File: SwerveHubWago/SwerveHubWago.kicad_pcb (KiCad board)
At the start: 2 copper layers, 84.5 x 32 mm, 5 parts, among them J1 2601-1110, J2 2601-1104, J3 15-91-3024

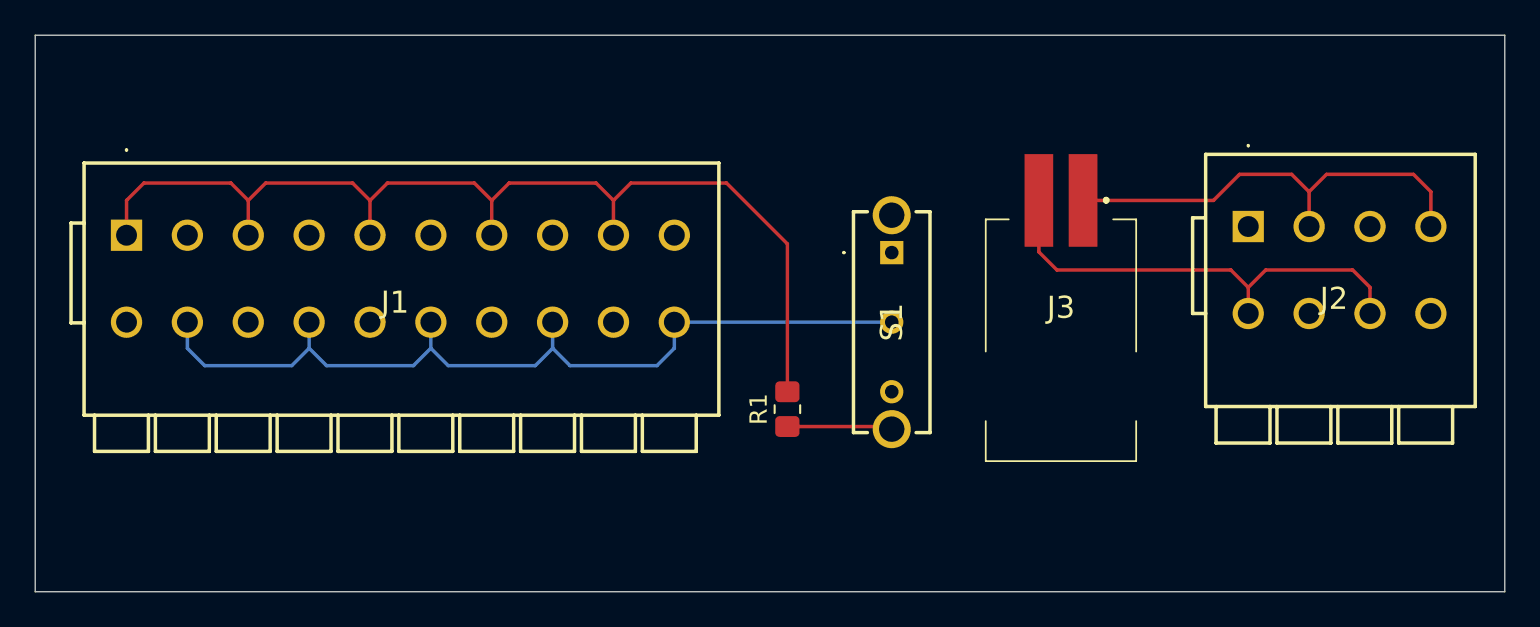
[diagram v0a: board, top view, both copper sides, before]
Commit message: Rev 2
Switched connecters to two (in/out) Molex SL connectors for CAN and one three pin Molex SL connector for power. Changed Wago terminal blocks to 6 position for CAN and 2 position for power.
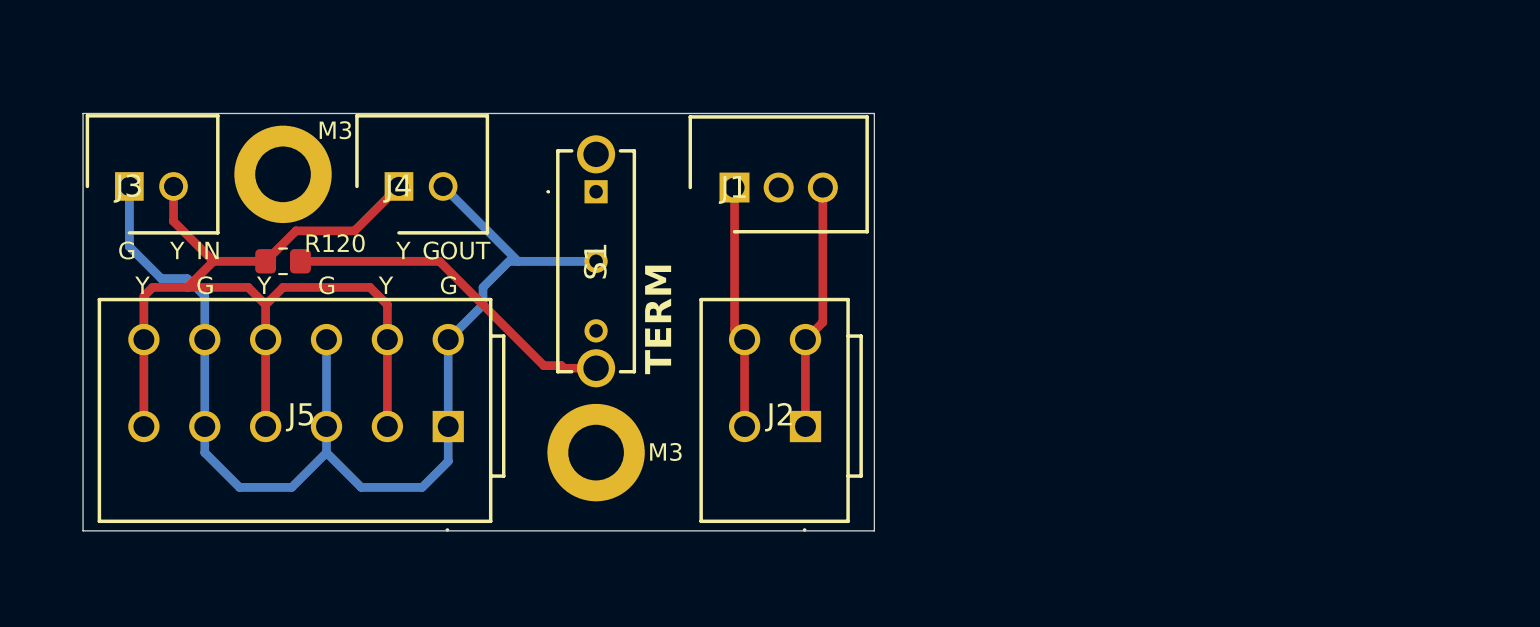
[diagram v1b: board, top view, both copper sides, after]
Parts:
- added J4: 70543-0036, SamacSys_Parts:SHDR2W64P0X254_1X2_737X660X1194P, F.Cu at (144.7, 44.2)
- added J5: 2601-3106, SamacSys_Parts:26013106, F.Cu at (147.5, 58.0)
- added M3: MountingHole_3.2mm_M3_DIN965_Pad, MountingHole:MountingHole_3.2mm_M3_DIN965_Pad, F.Cu at (156.0, 59.5)
- added M3: MountingHole_3.2mm_M3_DIN965_Pad, MountingHole:MountingHole_3.2mm_M3_DIN965_Pad, F.Cu at (138.0, 43.5)
- J1: value 2601-1110 -> 70543-0037; footprint SamacSys_Parts:26011110 -> SamacSys_Parts:SHDR3W97P0X254_1X3_1017X660X1181P
- J2: value 2601-1104 -> 2601-3102; footprint SamacSys_Parts:26011104 -> SamacSys_Parts:26013102
- J3: value 15-91-3024 -> 70543-0036; footprint SamacSys_Parts:15913024 -> SamacSys_Parts:SHDR2W64P0X254_1X2_737X660X1194P
- R120: renamed from R1; value R -> R120
- moved J3 54.8 mm to (129.2, 44.2)
- moved J1 35.1 mm to (164.0, 44.3)
- moved R120 30.2 mm to (138.0, 48.5), turned to 180 degrees
- moved J2 26.3 mm to (168.0, 53.0), turned to 180 degrees
- moved S1 17.4 mm to (156.0, 44.5)
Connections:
- J1 pad 1: /CAN-Y -> /PWR
- J1 pad 3: unconnected-(J1-2.1-Pad3) -> /GND
- J2 pad 1: unconnected-(J2-1.1-Pad1) -> /GND
- J2 pad 4: unconnected-(J2-2.2-Pad4) -> /PWR
- J3 pad 1: /PWR -> /CAN-G
- J3 pad 2: /GND -> /CAN-Y
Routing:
- net /CAN-G: track 51.3 -> 65.6 mm
- net Net-(S1-MH2): track 6.06 -> 19.5 mm
- net /GND: track 26.7 -> 14.2 mm
- net /PWR: track 25.9 -> 14.0 mm
- net /CAN-Y: track 62.2 -> 56.8 mm
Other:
- board size 84.5 x 32 mm -> 45.5 x 24 mm
- board text added: "${Name} - ${Rev}"
- board text added: "${REVISION}"
- board text added: "${TITLE}"
- board text added: "G"
- board text added: "IN"
- board text added: "OUT"
- board text added: "TERM"
- board text added: "Y"

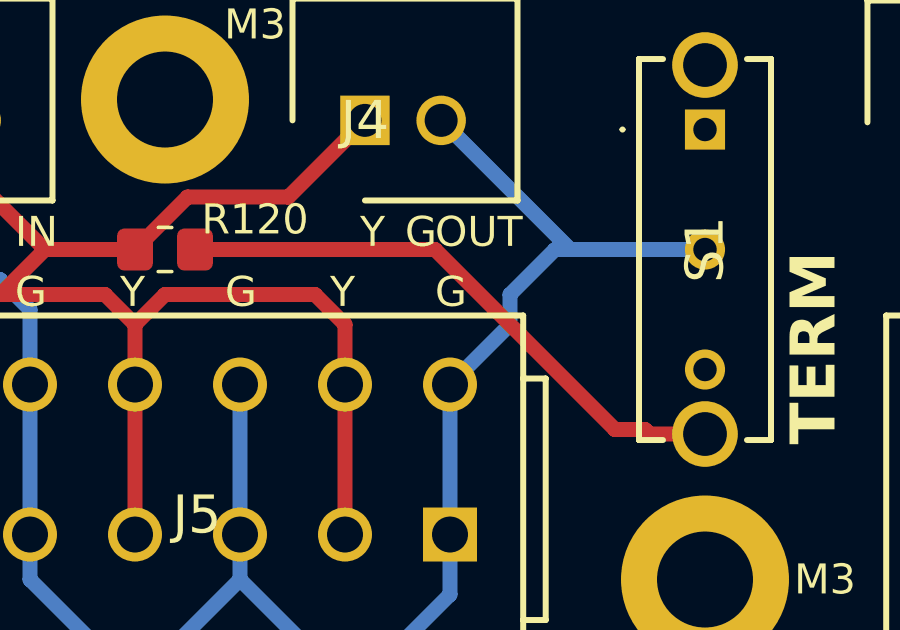
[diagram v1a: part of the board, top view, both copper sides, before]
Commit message: Fixed switch connections
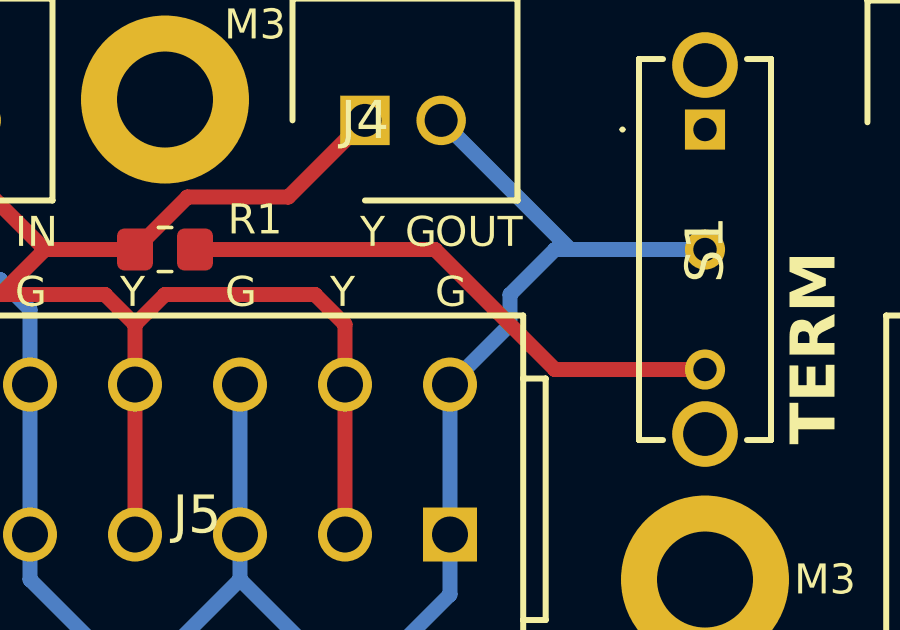
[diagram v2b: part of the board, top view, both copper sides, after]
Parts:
- renumbered R120 to R1
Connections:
- R1 pad 1: Net-(S1-MH2) -> Net-(S1-NO)
- S1 pad 3: unconnected-(S1-NO-Pad3) -> Net-(S1-NO)
- S1 pad 5: Net-(S1-MH2) -> unconnected-(S1-MH2-Pad5)
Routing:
- net Net-(S1-MH2): track 19.5 -> 0.00 mm
- net Net-(S1-NO): track 0.00 -> 18.7 mm
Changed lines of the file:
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@@
 	(net 3 "/GND")
 	(net 4 "/PWR")
-	(net 5 "Net-(S1-MH2)")
+	(net 5 "Net-(S1-NO)")
 	(net 6 "unconnected-(S1-MH1-Pad4)")
-	(net 7 "unconnected-(S1-NO-Pad3)")
+	(net 7 "unconnected-(S1-MH2-Pad5)")
 	(net 8 "unconnected-(S1-NC-Pad1)")
 	(net 9 "unconnected-(J1-Pad2)")
@@
 			(layers "*.Cu" "*.Mask" "F.SilkS")
 			(remove_unused_layers no)
-			(net 7 "unconnected-(S1-NO-Pad3)")
+			(net 5 "Net-(S1-NO)")
 			(pinfunction "NO")
 			(pintype "passive")
@@
 			(layers "*.Cu" "*.Mask" "F.SilkS")
 			(remove_unused_layers no)
-			(net 5 "Net-(S1-MH2)")
+			(net 7 "unconnected-(S1-MH2-Pad5)")
 			(pinfunction "MH2")
 			(pintype "passive")
@@
 		(descr "Resistor SMD 0805 (2012 Metric), square (rectangular) end terminal, IPC_7351 nominal with elongated pad for handsoldering. (Body size source: IPC-SM-782 page 72, https://www.pcb-3d.com/wordpress/wp-content/uploads/ipc-sm-782a_amendment_1_and_2.pdf), generated with kicad-footprint-generator")
 		(tags "resistor handsolder")
-		(property "Reference" "R120"
+		(property "Reference" "R1"
 			(at -3 1 0)
 			(layer "F.SilkS")
@@
 			(layers "F.Cu" "F.Paste" "F.Mask")
 			(roundrect_rratio 0.208333)
-			(net 5 "Net-(S1-MH2)")
+			(net 5 "Net-(S1-NO)")
 			(pintype "passive")
 		)
@@
 	)
 	(segment
-		(start 153 54.5)
-		(end 154 54.5)
-		(width 0.5)
-		(layer "F.Cu")
-		(net 5)
-	)
-	(segment
-		(start 154 54.5)
-		(end 154.15 54.65)
-		(width 0.5)
-		(layer "F.Cu")
-		(net 5)
-	)
-	(segment
 		(start 147 48.5)
-		(end 153 54.5)
+		(end 151 52.5)
 		(width 0.5)
 		(layer "F.Cu")
@@
 	)
 	(segment
-		(start 154.15 54.65)
-		(end 156 54.65)
+		(start 139 48.5)
+		(end 147 48.5)
 		(width 0.5)
 		(layer "F.Cu")
@@
 	)
 	(segment
-		(start 139 48.5)
-		(end 147 48.5)
+		(start 151 52.5)
+		(end 156 52.5)
 		(width 0.5)
 		(layer "F.Cu")
